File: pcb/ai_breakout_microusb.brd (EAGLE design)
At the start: 10.2 x 10.2 mm, 3 parts, among them J1 1X04NOSILK

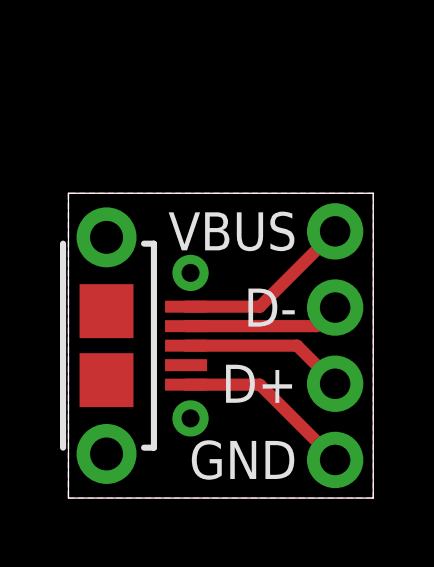
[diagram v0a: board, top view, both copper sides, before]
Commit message: redesigned to DIL form factor
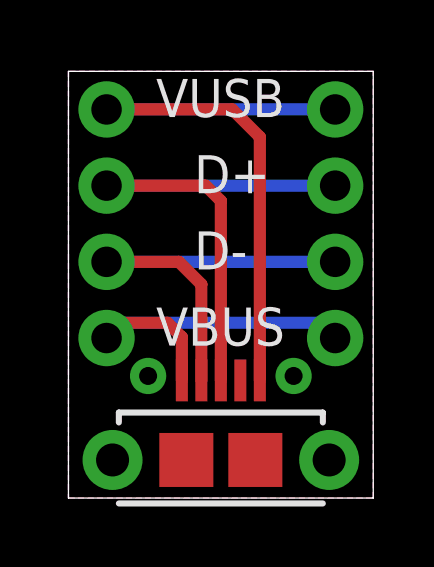
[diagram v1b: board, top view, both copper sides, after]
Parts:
- added J2: 1X04NFNS, Ai_Connectors:1X04-NFNS
- J1: value 1X04NOSILK -> 1X04NFNS; device Ai_Connectors:1X04-NOSILK -> Ai_Connectors:1X04-NFNS
- U$1: value AI-LOGOXS -> (none)
- moved U$1 8.72 mm to (6.99, 9.78), turned to 270 degrees
- moved J1 8.64 mm to (1.27, 9.14)
- moved USB1 5.39 mm to (5.08, 1.27), turned to 0 degrees
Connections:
- net D+: now also J1.3, J2.3; no longer J1.2
- net D-: now also J1.2, J2.2; no longer J1.3
- net GND: now also J1.4, J2.4; no longer J1.1
- net VBUS: now also J1.1, J2.1; no longer J1.4
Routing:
- net GND: track 6.01 -> 21.2 mm
- net D+: track 5.50 -> 17.6 mm
- net D-: track 5.23 -> 14.3 mm
- net VBUS: track 6.01 -> 12.4 mm
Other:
- board size 10.2 x 10.2 mm -> 10.2 x 14.2 mm
- board text added: "Micro-USB Breakout"
- board text added: "Pasadena, CA"
- board text added: "VUSB"
- board text removed: "GND"
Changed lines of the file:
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@@
 <setting verticaltext="up"/>
 </settings>
-<grid distance="25" unitdist="mil" unit="mil" style="lines" multiple="1" display="yes" altdistance="0.025" altunitdist="inch" altunit="inch"/>
+<grid distance="5" unitdist="mil" unit="mil" style="lines" multiple="1" display="yes" altdistance="0.025" altunitdist="inch" altunit="inch"/>
 <layers>
 <layer number="1" name="Top" color="4" fill="1" visible="yes" active="yes"/>
@@
 <board>
 <plain>
+<wire x1="10.16" y1="0" x2="10.16" y2="14.224" width="0.0254" layer="20"/>
+<wire x1="10.16" y1="14.224" x2="0" y2="14.224" width="0.0254" layer="20"/>
+<wire x1="0" y1="14.224" x2="0" y2="0" width="0.0254" layer="20"/>
 <wire x1="0" y1="0" x2="10.16" y2="0" width="0.0254" layer="20"/>
-<wire x1="10.16" y1="0" x2="10.16" y2="10.16" width="0.0254" layer="20"/>
-<wire x1="10.16" y1="10.16" x2="0" y2="10.16" width="0.0254" layer="20"/>
-<wire x1="0" y1="10.16" x2="0" y2="0" width="0.0254" layer="20"/>
-<text x="7.62" y="9.525" size="1.27" layer="25" font="vector" ratio="15" rot="R180">VBUS</text>
-<text x="7.62" y="6.985" size="1.27" layer="25" font="vector" ratio="15" rot="R180">D-</text>
-<text x="7.62" y="4.445" size="1.27" layer="25" font="vector" ratio="15" rot="R180">D+</text>
-<text x="7.62" y="1.905" size="1.27" layer="25" font="vector" ratio="15" rot="R180">GND</text>
-<text x="3.175" y="9.525" size="1.27" layer="26" font="vector" ratio="15" rot="MR180">VBUS</text>
-<text x="7.62" y="5.715" size="1.27" layer="26" font="vector" ratio="15" rot="MR0">D-</text>
-<text x="7.62" y="3.175" size="1.27" layer="26" font="vector" ratio="15" rot="MR0">D+</text>
-<text x="7.62" y="0.635" size="1.27" layer="26" font="vector" ratio="15" rot="MR0">GND</text>
+<text x="7.366" y="12.7" size="1.27" layer="26" font="vector" ratio="10" rot="MR0">VUSB</text>
+<text x="6.223" y="10.16" size="1.27" layer="26" font="vector" ratio="10" rot="MR0">D+</text>
+<text x="2.921" y="12.7" size="1.27" layer="25" font="vector" ratio="10" rot="SR0">VUSB</text>
+<text x="4.191" y="10.16" size="1.27" layer="25" font="vector" ratio="10" rot="SR0">D+</text>
+<text x="6.223" y="7.62" size="1.27" layer="26" font="vector" ratio="10" rot="MR0">D-</text>
+<text x="4.191" y="7.62" size="1.27" layer="25" font="vector" ratio="10" rot="SR0">D-</text>
+<text x="7.747" y="11.303" size="0.6096" layer="26" font="vector" ratio="10" rot="SMR270">Pasadena, CA</text>
+<text x="2.921" y="5.08" size="1.27" layer="25" font="vector" ratio="10" rot="SR0">VBUS</text>
+<text x="7.239" y="5.08" size="1.27" layer="26" font="vector" ratio="10" rot="MR0">D-</text>
+<text x="7.239" y="5.08" size="1.27" layer="26" font="vector" ratio="10" rot="MR0">VBUS</text>
+<text x="3.048" y="8.382" size="0.6096" layer="26" font="vector" ratio="10" rot="SMR270" align="center">Micro-USB
+Breakout</text>
 </plain>
 <attributes>
@@
 </autorouter>
 <elements>
-<element name="J1" library="Ai_Connectors" package="1X04-NOSILK" value="1X04NOSILK" x="8.89" y="5.08" smashed="yes" rot="R90"/>
-<element name="U$1" library="Ai_Miscellany" package="AI-LOGO-XS" value="AI-LOGOXS" x="0.635" y="3.81" rot="MR90"/>
-<element name="USB1" library="Ai_Connectors" package="USB-MICROB-TH" value="USBMICROB-TH" x="1.27" y="5.08" smashed="yes" rot="R270"/>
+<element name="U$1" library="Ai_Miscellany" package="AI-LOGO-XS" value="" x="6.985" y="9.779" rot="MR270"/>
+<element name="J1" library="Ai_Connectors" package="1X04-NFNS" value="1X04NFNS" x="1.27" y="9.144" smashed="yes" rot="R90"/>
+<element name="J2" library="Ai_Connectors" package="1X04-NFNS" value="1X04NFNS" x="8.89" y="9.144" smashed="yes" rot="R90"/>
+<element name="USB1" library="Ai_Connectors" package="USB-MICROB-TH" value="USBMICROB-TH" x="5.08" y="1.27"/>
 </elements>
 <signals>
-<signal name="D+">
-<contactref element="USB1" pad="D+"/>
-<contactref element="J1" pad="2"/>
-<wire x1="8.89" y1="3.81" x2="7.62" y2="5.08" width="0.4064" layer="1"/>
-<wire x1="7.62" y1="5.08" x2="3.92" y2="5.08" width="0.4064" layer="1"/>
+<signal name="GND">
+<polygon width="0.254" layer="16">
+<vertex x="10.16" y="0"/>
+<vertex x="10.16" y="14.224"/>
+<vertex x="0" y="14.224"/>
+<vertex x="0" y="0"/>
+</polygon>
+<polygon width="0.254" layer="1">
+<vertex x="10.16" y="0"/>
+<vertex x="10.16" y="14.224"/>
+<vertex x="0" y="14.224"/>
+<vertex x="0" y="0"/>
+</polygon>
+<contactref element="J1" pad="4"/>
+<contactref element="USB1" pad="GND"/>
+<contactref element="J2" pad="4"/>
+<wire x1="8.89" y1="12.954" x2="1.27" y2="12.954" width="0.4064" layer="16"/>
+<wire x1="6.38" y1="3.92" x2="6.38" y2="12.035" width="0.4064" layer="1"/>
+<wire x1="6.38" y1="12.035" x2="5.461" y2="12.954" width="0.4064" layer="1"/>
+<wire x1="5.461" y1="12.954" x2="1.27" y2="12.954" width="0.4064" layer="1"/>
+</signal>
+<signal name="VBUS">
+<contactref element="USB1" pad="VBUS"/>
+<contactref element="J2" pad="1"/>
+<contactref element="J1" pad="1"/>
+<wire x1="8.89" y1="5.334" x2="8.382" y2="5.842" width="0.4064" layer="16"/>
+<wire x1="8.382" y1="5.842" x2="1.778" y2="5.842" width="0.4064" layer="16"/>
+<wire x1="1.778" y1="5.842" x2="1.27" y2="5.334" width="0.4064" layer="16"/>
+<wire x1="3.78" y1="3.92" x2="3.78" y2="5.364" width="0.4064" layer="1"/>
+<wire x1="3.78" y1="5.364" x2="3.302" y2="5.842" width="0.4064" layer="1"/>
+<wire x1="3.302" y1="5.842" x2="1.778" y2="5.842" width="0.4064" layer="1"/>
+<wire x1="1.778" y1="5.842" x2="1.27" y2="5.334" width="0.4064" layer="1"/>
 </signal>
 <signal name="D-">
 <contactref element="USB1" pad="D-"/>
+<contactref element="J2" pad="2"/>
+<contactref element="J1" pad="2"/>
+<wire x1="8.89" y1="7.874" x2="1.27" y2="7.874" width="0.4064" layer="16"/>
+<wire x1="4.43" y1="3.92" x2="4.43" y2="7.127" width="0.4064" layer="1"/>
+<wire x1="4.43" y1="7.127" x2="3.683" y2="7.874" width="0.4064" layer="1"/>
+<wire x1="3.683" y1="7.874" x2="1.27" y2="7.874" width="0.4064" layer="1"/>
+</signal>
+<signal name="D+">
+<contactref element="J2" pad="3"/>
+<contactref element="USB1" pad="D+"/>
 <contactref element="J1" pad="3"/>
-<wire x1="8.89" y1="6.35" x2="8.27" y2="5.73" width="0.4064" layer="1"/>
-<wire x1="8.27" y1="5.73" x2="3.92" y2="5.73" width="0.4064" layer="1"/>
-</signal>
-<signal name="VBUS">
-<contactref element="USB1" pad="VBUS"/>
-<contactref element="J1" pad="4"/>
-<wire x1="8.89" y1="8.89" x2="6.38" y2="6.38" width="0.4064" layer="1"/>
-<wire x1="6.38" y1="6.38" x2="3.92" y2="6.38" width="0.4064" layer="1"/>
-</signal>
-<signal name="GND">
-<polygon width="0.254" layer="16">
-<vertex x="0" y="0"/>
-<vertex x="10.16" y="0"/>
-<vertex x="10.16" y="10.16"/>
-<vertex x="0" y="10.16"/>
-</polygon>
-<polygon width="0.254" layer="1">
-<vertex x="0" y="0"/>
-<vertex x="10.16" y="0"/>
-<vertex x="10.16" y="10.16"/>
-<vertex x="0" y="10.16"/>
-</polygon>
-<contactref element="USB1" pad="GND"/>
-<contactref element="J1" pad="1"/>
-<wire x1="8.89" y1="1.27" x2="6.38" y2="3.78" width="0.4064" layer="1"/>
-<wire x1="6.38" y1="3.78" x2="3.92" y2="3.78" width="0.4064" layer="1"/>
-</signal>
-<signal name="D+1">
+<wire x1="8.89" y1="10.414" x2="1.27" y2="10.414" width="0.4064" layer="16"/>
+<wire x1="5.08" y1="3.92" x2="5.08" y2="9.906" width="0.4064" layer="1"/>
+<wire x1="5.08" y1="9.906" x2="4.572" y2="10.414" width="0.4064" layer="1"/>
+<wire x1="4.572" y1="10.414" x2="1.27" y2="10.414" width="0.4064" layer="1"/>
 </signal>
 </signals>
 </board>
 </drawing>
+<compatibility>
+<note version="6.3" minversion="6.2.2" severity="warning">
+Since Version 6.2.2 text objects can contain more than one line,
+which will not be processed correctly with this version.
+</note>
+</compatibility>
 </eagle>

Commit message: updated silkscreen
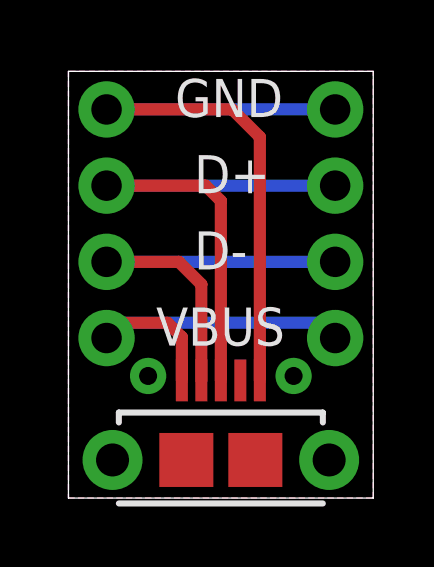
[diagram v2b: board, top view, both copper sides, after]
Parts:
- moved U$1 8.90 mm to (6.48, 0.89), turned to 0 degrees
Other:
- board text added: "GND"
- board text removed: "VUSB"
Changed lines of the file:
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@@
 <setting verticaltext="up"/>
 </settings>
-<grid distance="5" unitdist="mil" unit="mil" style="lines" multiple="1" display="yes" altdistance="0.025" altunitdist="inch" altunit="inch"/>
+<grid distance="50" unitdist="mil" unit="mil" style="lines" multiple="1" display="yes" altdistance="0.025" altunitdist="inch" altunit="inch"/>
 <layers>
 <layer number="1" name="Top" color="4" fill="1" visible="yes" active="yes"/>
@@
 <wire x1="0" y1="14.224" x2="0" y2="0" width="0.0254" layer="20"/>
 <wire x1="0" y1="0" x2="10.16" y2="0" width="0.0254" layer="20"/>
-<text x="7.366" y="12.7" size="1.27" layer="26" font="vector" ratio="10" rot="MR0">VUSB</text>
+<text x="6.731" y="12.7" size="1.27" layer="26" font="vector" ratio="10" rot="MR0">GND</text>
 <text x="6.223" y="10.16" size="1.27" layer="26" font="vector" ratio="10" rot="MR0">D+</text>
-<text x="2.921" y="12.7" size="1.27" layer="25" font="vector" ratio="10" rot="SR0">VUSB</text>
+<text x="3.556" y="12.7" size="1.27" layer="25" font="vector" ratio="10" rot="SR0">GND</text>
 <text x="4.191" y="10.16" size="1.27" layer="25" font="vector" ratio="10" rot="SR0">D+</text>
 <text x="6.223" y="7.62" size="1.27" layer="26" font="vector" ratio="10" rot="MR0">D-</text>
 <text x="4.191" y="7.62" size="1.27" layer="25" font="vector" ratio="10" rot="SR0">D-</text>
-<text x="7.747" y="11.303" size="0.6096" layer="26" font="vector" ratio="10" rot="SMR270">Pasadena, CA</text>
+<text x="7.747" y="13.081" size="0.6096" layer="26" font="vector" ratio="10" rot="SMR270">Pasadena, CA</text>
 <text x="2.921" y="5.08" size="1.27" layer="25" font="vector" ratio="10" rot="SR0">VBUS</text>
-<text x="7.239" y="5.08" size="1.27" layer="26" font="vector" ratio="10" rot="MR0">D-</text>
 <text x="7.239" y="5.08" size="1.27" layer="26" font="vector" ratio="10" rot="MR0">VBUS</text>
-<text x="3.048" y="8.382" size="0.6096" layer="26" font="vector" ratio="10" rot="SMR270" align="center">Micro-USB
+<text x="7.239" y="5.08" size="1.27" layer="26" font="vector" ratio="10" rot="MR0">VBUS</text>
+<text x="3.048" y="10.16" size="0.6096" layer="26" font="vector" ratio="10" rot="SMR270" align="center">Micro-USB
 Breakout</text>
 </plain>
@@
 </autorouter>
 <elements>
-<element name="U$1" library="Ai_Miscellany" package="AI-LOGO-XS" value="" x="6.985" y="9.779" rot="MR270"/>
+<element name="U$1" library="Ai_Miscellany" package="AI-LOGO-XS" value="" x="6.477" y="0.889" rot="MR0"/>
 <element name="J1" library="Ai_Connectors" package="1X04-NFNS" value="1X04NFNS" x="1.27" y="9.144" smashed="yes" rot="R90"/>
 <element name="J2" library="Ai_Connectors" package="1X04-NFNS" value="1X04NFNS" x="8.89" y="9.144" smashed="yes" rot="R90"/>
